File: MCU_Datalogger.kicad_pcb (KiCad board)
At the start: 2 copper layers, 50.2 x 30.2 mm, 30 parts, among them J1 Conn_01x04_Male, J2 Conn_01x04_Male, J3 Conn_01x09_Male, J4 Conn_02x03_Odd_Even, U1 DS1337S+, U2 24LC1025, U3 24LC1025, U4 ATMEGA328P-AU, Y1 32.768 KHz, Y2 16 MHz

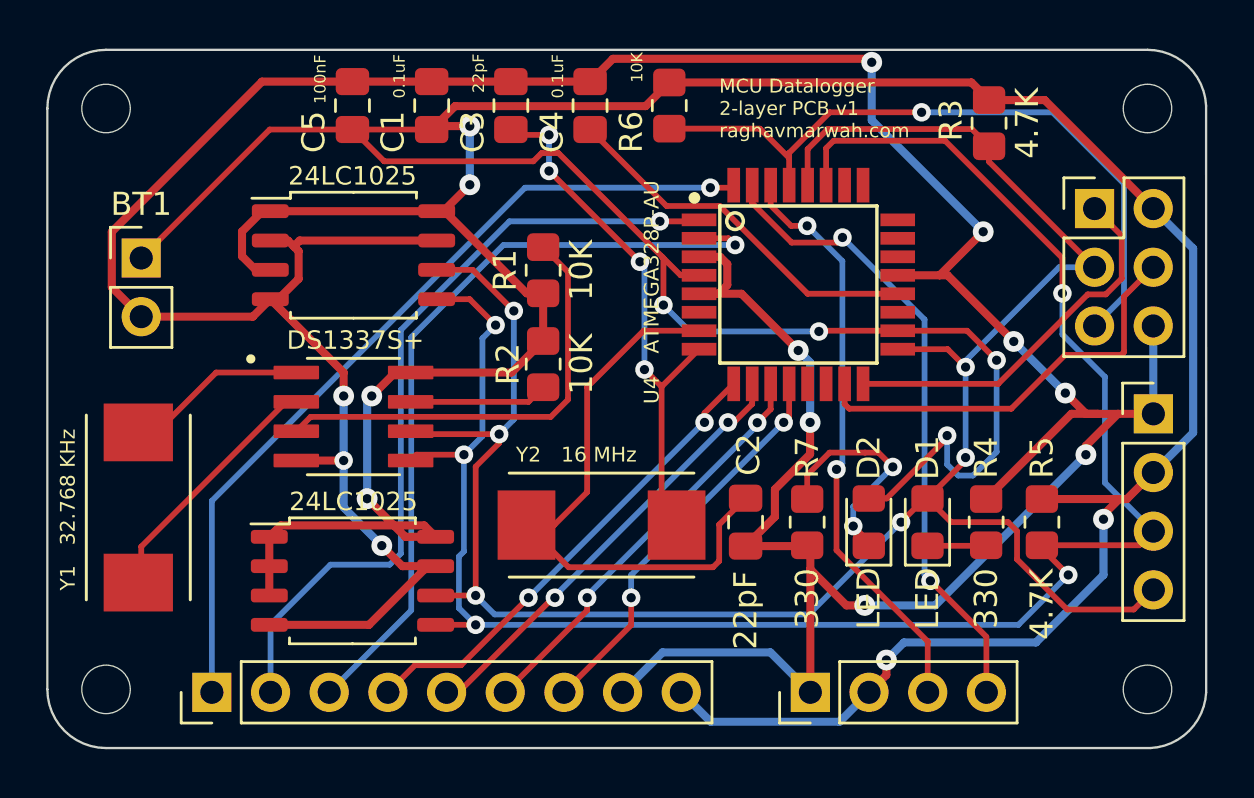
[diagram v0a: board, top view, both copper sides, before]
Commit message: Minor changes to PCB footprints
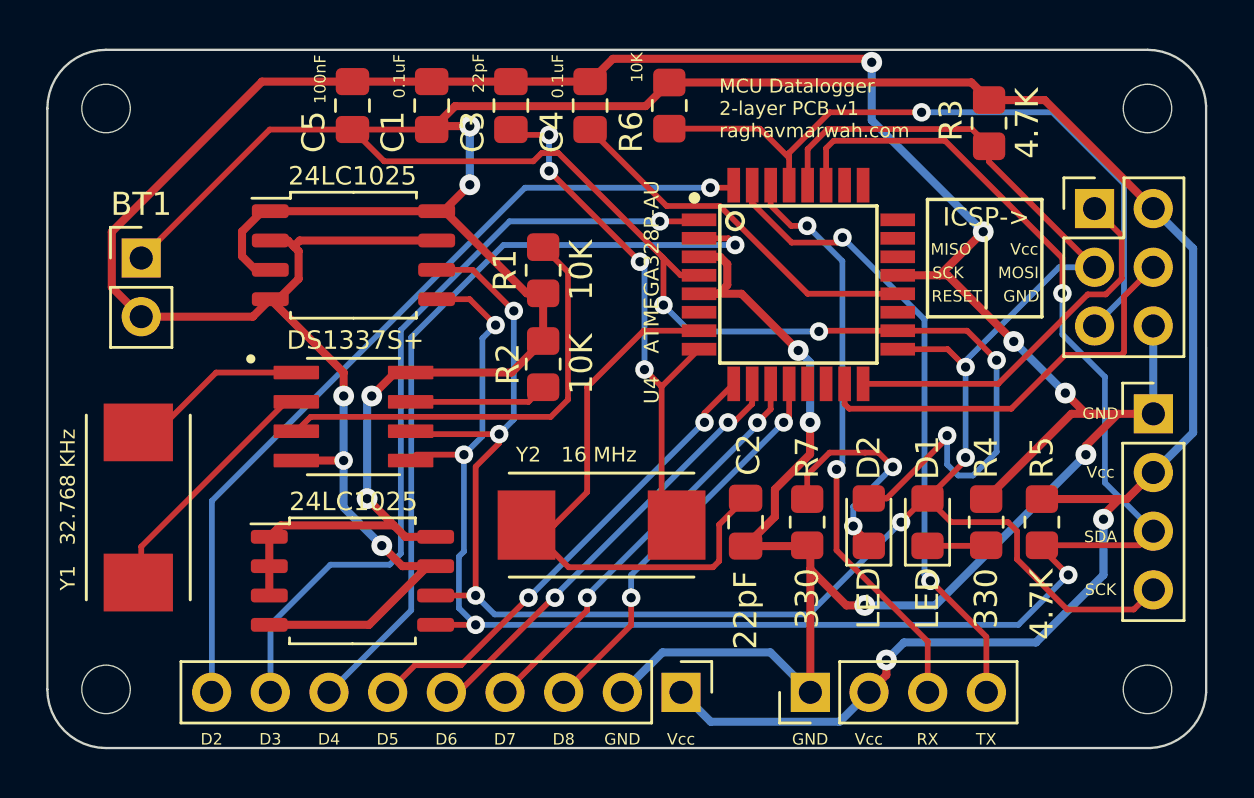
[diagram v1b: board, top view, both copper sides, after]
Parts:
- moved J3 20.3 mm to (153.3, 114.8), turned to -90 degrees
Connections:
- J3 pad 1: /D2 -> /Vcc
- J3 pad 2: /D3 -> GND
- J3 pad 3: /D4 -> /D8
- J3 pad 4: /D5 -> /D7
- J3 pad 6: /D7 -> /D5
- J3 pad 7: /D8 -> /D4
- J3 pad 8: GND -> /D3
- J3 pad 9: /Vcc -> /D2
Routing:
- net /Vcc: track 193.5 -> 191.5 mm
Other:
- board text added: "D2"
- board text added: "D3"
- board text added: "D4"
- board text added: "D5"
- board text added: "D6"
- board text added: "D7"
- board text added: "D8"
- board text added: "GND"
- board text added: "ICSP->"
- board text added: "MISO"
- board text added: "MOSI"
- board text added: "RESET"
- board text added: "RX"
- board text added: "SCK"
- board text added: "SDA"
- board text added: "TX"
- board text added: "Vcc"
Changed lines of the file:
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@@
   )
   (footprint "Connector_PinHeader_2.54mm:PinHeader_1x09_P2.54mm_Vertical" (layer "F.Cu")
-    (at 132.979 114.808 90)
+    (at 153.289 114.808 -90)
     (descr "Through hole straight pin header, 1x09, 2.54mm pitch, single row")
     (tags "Through hole pin header THT 1x09 2.54mm single row")
@@
     (fp_line (start -1.27 -0.635) (end -0.635 -1.27) (layer "F.Fab") (width 0.1))
     (fp_line (start -1.27 21.59) (end -1.27 -0.635) (layer "F.Fab") (width 0.1))
-    (pad "1" thru_hole rect (at 0 0 90) (size 1.7 1.7) (drill 1) (layers *.Cu *.Mask)
-      (net 12 "/D2") (pinfunction "Pin_1") (pintype "passive"))
-    (pad "2" thru_hole oval (at 0 2.54 90) (size 1.7 1.7) (drill 1) (layers *.Cu *.Mask)
-      (net 13 "/D3") (pinfunction "Pin_2") (pintype "passive"))
-    (pad "3" thru_hole oval (at 0 5.08 90) (size 1.7 1.7) (drill 1) (layers *.Cu *.Mask)
-      (net 14 "/D4") (pinfunction "Pin_3") (pintype "passive"))
-    (pad "4" thru_hole oval (at 0 7.62 90) (size 1.7 1.7) (drill 1) (layers *.Cu *.Mask)
-      (net 15 "/D5") (pinfunction "Pin_4") (pintype "passive"))
-    (pad "5" thru_hole oval (at 0 10.16 90) (size 1.7 1.7) (drill 1) (layers *.Cu *.Mask)
+    (pad "1" thru_hole rect (at 0 0 270) (size 1.7 1.7) (drill 1) (layers *.Cu *.Mask)
+      (net 2 "/Vcc") (pinfunction "Pin_1") (pintype "passive"))
+    (pad "2" thru_hole oval (at 0 2.54 270) (size 1.7 1.7) (drill 1) (layers *.Cu *.Mask)
+      (net 1 "GND") (pinfunction "Pin_2") (pintype "passive"))
+    (pad "3" thru_hole oval (at 0 5.08 270) (size 1.7 1.7) (drill 1) (layers *.Cu *.Mask)
+      (net 18 "/D8") (pinfunction "Pin_3") (pintype "passive"))
+    (pad "4" thru_hole oval (at 0 7.62 270) (size 1.7 1.7) (drill 1) (layers *.Cu *.Mask)
+      (net 17 "/D7") (pinfunction "Pin_4") (pintype "passive"))
+    (pad "5" thru_hole oval (at 0 10.16 270) (size 1.7 1.7) (drill 1) (layers *.Cu *.Mask)
       (net 16 "/D6") (pinfunction "Pin_5") (pintype "passive"))
-    (pad "6" thru_hole oval (at 0 12.7 90) (size 1.7 1.7) (drill 1) (layers *.Cu *.Mask)
-      (net 17 "/D7") (pinfunction "Pin_6") (pintype "passive"))
-    (pad "7" thru_hole oval (at 0 15.24 90) (size 1.7 1.7) (drill 1) (layers *.Cu *.Mask)
-      (net 18 "/D8") (pinfunction "Pin_7") (pintype "passive"))
-    (pad "8" thru_hole oval (at 0 17.78 90) (size 1.7 1.7) (drill 1) (layers *.Cu *.Mask)
-      (net 1 "GND") (pinfunction "Pin_8") (pintype "passive"))
-    (pad "9" thru_hole oval (at 0 20.32 90) (size 1.7 1.7) (drill 1) (layers *.Cu *.Mask)
-      (net 2 "/Vcc") (pinfunction "Pin_9") (pintype "passive"))
+    (pad "6" thru_hole oval (at 0 12.7 270) (size 1.7 1.7) (drill 1) (layers *.Cu *.Mask)
+      (net 15 "/D5") (pinfunction "Pin_6") (pintype "passive"))
+    (pad "7" thru_hole oval (at 0 15.24 270) (size 1.7 1.7) (drill 1) (layers *.Cu *.Mask)
+      (net 14 "/D4") (pinfunction "Pin_7") (pintype "passive"))
+    (pad "8" thru_hole oval (at 0 17.78 270) (size 1.7 1.7) (drill 1) (layers *.Cu *.Mask)
+      (net 13 "/D3") (pinfunction "Pin_8") (pintype "passive"))
+    (pad "9" thru_hole oval (at 0 20.32 270) (size 1.7 1.7) (drill 1) (layers *.Cu *.Mask)
+      (net 12 "/D2") (pinfunction "Pin_9") (pintype "passive"))
     (model "${KICAD6_3DMODEL_DIR}/Connector_PinHeader_2.54mm.3dshapes/PinHeader_1x09_P2.54mm_Vertical.wrl"
       (offset (xyz 0 0 0))
@@
       ) (layer "B.SilkS") (width 0.01) (fill solid))
   )
+  (gr_line (start 166.497 95.123) (end 166.497 98.171) (layer "F.SilkS") (width 0.15))
+  (gr_rect (start 163.957 93.472) (end 168.91 98.552) (layer "F.SilkS") (width 0.15) (fill none))
   (gr_arc (start 125.857 89.535) (mid 126.600949 87.738949) (end 128.397 86.995) (layer "Edge.Cuts") (width 0.1))
   (gr_line (start 125.857 89.535) (end 125.857 114.681) (layer "Edge.Cuts") (width 0.1))
@@
   (gr_line (start 128.397 117.221) (end 173.609 117.221) (layer "Edge.Cuts") (width 0.1))
   (gr_rect (start 125.857 86.995) (end 175.9966 117.1956) (layer "User.2") (width 0.1) (fill none))
+  (gr_text "MOSI" (at 167.894 96.647) (layer "F.SilkS")
+    (effects (font (size 0.5 0.5) (thickness 0.08)))
+  )
+  (gr_text "GND" (at 168.021 97.663) (layer "F.SilkS")
+    (effects (font (size 0.5 0.5) (thickness 0.08)))
+  )
+  (gr_text "TX" (at 166.497 116.84) (layer "F.SilkS")
+    (effects (font (size 0.5 0.5) (thickness 0.1)))
+  )
+  (gr_text "GND\n" (at 158.877 116.84) (layer "F.SilkS")
+    (effects (font (size 0.5 0.5) (thickness 0.1)))
+  )
+  (gr_text "Vcc" (at 168.148 95.631) (layer "F.SilkS")
+    (effects (font (size 0.5 0.5) (thickness 0.08)))
+  )
+  (gr_text "Vcc" (at 153.289 116.84) (layer "F.SilkS")
+    (effects (font (size 0.5 0.5) (thickness 0.1)))
+  )
+  (gr_text "MISO" (at 164.973 95.631) (layer "F.SilkS")
+    (effects (font (size 0.5 0.5) (thickness 0.08)))
+  )
+  (gr_text "SDA" (at 171.45 108.077) (layer "F.SilkS")
+    (effects (font (size 0.5 0.5) (thickness 0.1)))
+  )
+  (gr_text "SCK" (at 171.45 110.363) (layer "F.SilkS")
+    (effects (font (size 0.5 0.5) (thickness 0.1)))
+  )
+  (gr_text "D2" (at 132.969 116.84) (layer "F.SilkS")
+    (effects (font (size 0.5 0.5) (thickness 0.1)))
+  )
+  (gr_text "GND\n" (at 171.45 102.743) (layer "F.SilkS")
+    (effects (font (size 0.5 0.5) (thickness 0.1)))
+  )
   (gr_text "MCU Datalogger\n2-layer PCB v1\nraghavmarwah.com" (at 154.94 89.535) (layer "F.SilkS")
     (effects (font (size 0.6 0.6) (thickness 0.12)) (justify left))
   )
+  (gr_text "GND\n" (at 150.749 116.84) (layer "F.SilkS")
+    (effects (font (size 0.5 0.5) (thickness 0.1)))
+  )
+  (gr_text "D8" (at 148.209 116.84) (layer "F.SilkS")
+    (effects (font (size 0.5 0.5) (thickness 0.1)))
+  )
+  (gr_text "RX" (at 163.957 116.84) (layer "F.SilkS")
+    (effects (font (size 0.5 0.5) (thickness 0.1)))
+  )
+  (gr_text "Vcc" (at 161.417 116.84) (layer "F.SilkS")
+    (effects (font (size 0.5 0.5) (thickness 0.1)))
+  )
+  (gr_text "D3" (at 135.509 116.84) (layer "F.SilkS")
+    (effects (font (size 0.5 0.5) (thickness 0.1)))
+  )
+  (gr_text "Vcc" (at 171.45 105.283) (layer "F.SilkS")
+    (effects (font (size 0.5 0.5) (thickness 0.1)))
+  )
+  (gr_text "ICSP->" (at 166.497 94.234) (layer "F.SilkS")
+    (effects (font (size 0.8 0.8) (thickness 0.1)))
+  )
+  (gr_text "D5" (at 140.589 116.84) (layer "F.SilkS")
+    (effects (font (size 0.5 0.5) (thickness 0.1)))
+  )
+  (gr_text "SCK" (at 164.846 96.647) (layer "F.SilkS")
+    (effects (font (size 0.5 0.5) (thickness 0.08)))
+  )
+  (gr_text "D7" (at 145.669 116.84) (layer "F.SilkS")
+    (effects (font (size 0.5 0.5) (thickness 0.1)))
+  )
+  (gr_text "RESET" (at 165.227 97.663) (layer "F.SilkS")
+    (effects (font (size 0.5 0.5) (thickness 0.08)))
+  )
+  (gr_text "D4" (at 138.049 116.84) (layer "F.SilkS")
+    (effects (font (size 0.5 0.5) (thickness 0.1)))
+  )
+  (gr_text "D6" (at 143.129 116.84) (layer "F.SilkS")
+    (effects (font (size 0.5 0.5) (thickness 0.1)))
+  )
   (segment (start 138.684 100.965) (end 138.684 101.981) (width 0.35) (layer "F.Cu") (net 1))
   (segment (start 164.827 96.755) (end 167.69199 99.61999) (width 0.35) (layer "F.Cu") (net 1))
@@
   (segment (start 164.8085 103.7965) (end 162.188 106.417) (width 0.25) (layer "F.Cu") (net 2))
   (segment (start 152.4635 95.9485) (end 153.27 96.755) (width 0.25) (layer "F.Cu") (net 2))
+  (segment (start 135.959 107.583) (end 135.465 108.077) (width 0.35) (layer "F.Cu") (net 2))
   (segment (start 151.756 89.433) (end 152.781 88.408) (width 0.35) (layer "F.Cu") (net 2))
   (segment (start 144.145 90.297) (end 142.6425 90.297) (width 0.35) (layer "F.Cu") (net 2))
@@
   (segment (start 143.052173 93.98) (end 146.608173 97.536) (width 0.35) (layer "F.Cu") (net 2))
   (segment (start 135.465 108.077) (end 135.465 110.617) (width 0.35) (layer "F.Cu") (net 2))
-  (segment (start 135.959 107.583) (end 135.465 108.077) (width 0.35) (layer "F.Cu") (net 2))
   (segment (start 159.29 99.155) (end 162.669 99.155) (width 0.25) (layer "F.Cu") (net 2))
   (segment (start 171.577 107.1245) (end 171.577 107.315) (width 0.35) (layer "F.Cu") (net 2))
@@
   (segment (start 147.252984 91.4645) (end 147.9795 91.4645) (width 0.25) (layer "F.Cu") (net 2))
   (segment (start 134.284 94.861827) (end 134.284 95.93) (width 0.35) (layer "F.Cu") (net 2))
-  (segment (start 142.665 108.077) (end 142.171 107.583) (width 0.35) (layer "F.Cu") (net 2))
   (segment (start 152.781 88.408) (end 165.862 88.408) (width 0.35) (layer "F.Cu") (net 2))
-  (segment (start 142.171 107.583) (end 135.959 107.583) (width 0.35) (layer "F.Cu") (net 2))
   (segment (start 142.709 93.98) (end 143.052173 93.98) (width 0.35) (layer "F.Cu") (net 2))
   (segment (start 135.509 93.98) (end 135.165827 93.98) (width 0.35) (layer "F.Cu") (net 2))
+  (segment (start 140.843 107.583) (end 135.959 107.583) (width 0.35) (layer "F.Cu") (net 2))
   (segment (start 139.7 106.426) (end 141.351 108.077) (width 0.35) (layer "F.Cu") (net 2))
   (segment (start 141.351 108.077) (end 142.665 108.077) (width 0.35) (layer "F.Cu") (net 2))

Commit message: Added SCL net to schematic and fixed errors
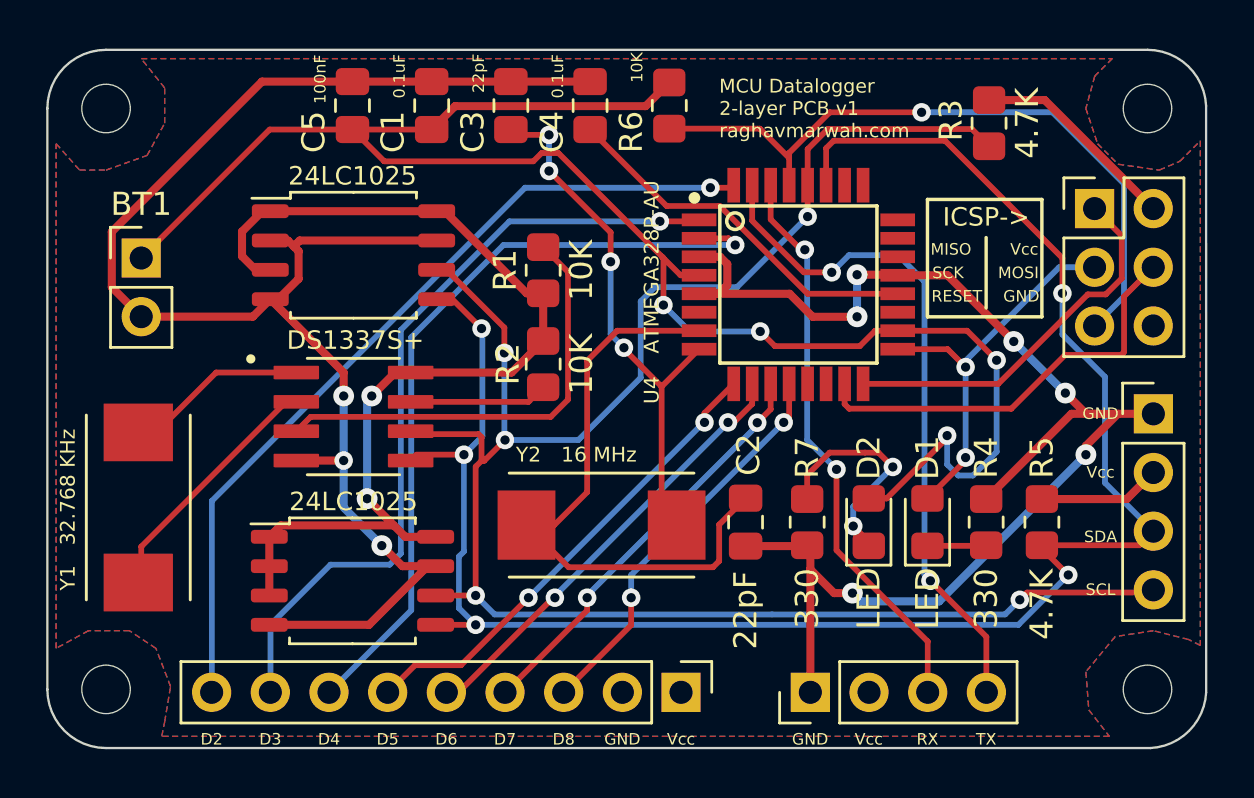
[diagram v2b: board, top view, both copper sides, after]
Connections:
- J1 pad 4: /SCK -> /SCL
- R3 pad 2: /SCK -> /SCL
- U1 pad 6: /SCK -> /SCL
- U2 pad 6: /SCK -> /SCL
- U3 pad 6: /SCK -> /SCL
- U4 pad 28: /SCK -> /SCL
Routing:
- net /SCL: track 0.00 -> 81.8 mm, vias 0 -> 5
- net /SCK: track 91.6 -> 16.9 mm, vias 6 -> 2
- net /Vcc: track 191.5 -> 133.6 mm, vias 10 -> 6
- net GND: track 173.1 -> 130.6 mm, vias 11 -> 9
- net /TX: track 27.8 -> 29.6 mm
- net /SDA: track 82.0 -> 81.1 mm
- net Net-(C2-Pad2): track 25.4 -> 26.0 mm
- net /RX: track 25.4 -> 24.9 mm
- added copper zone on F.Cu, net /Vcc
- added copper zone on B.Cu, net GND
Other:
- board text added: "SCL"

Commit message: Test commit, deleted tracks and vias
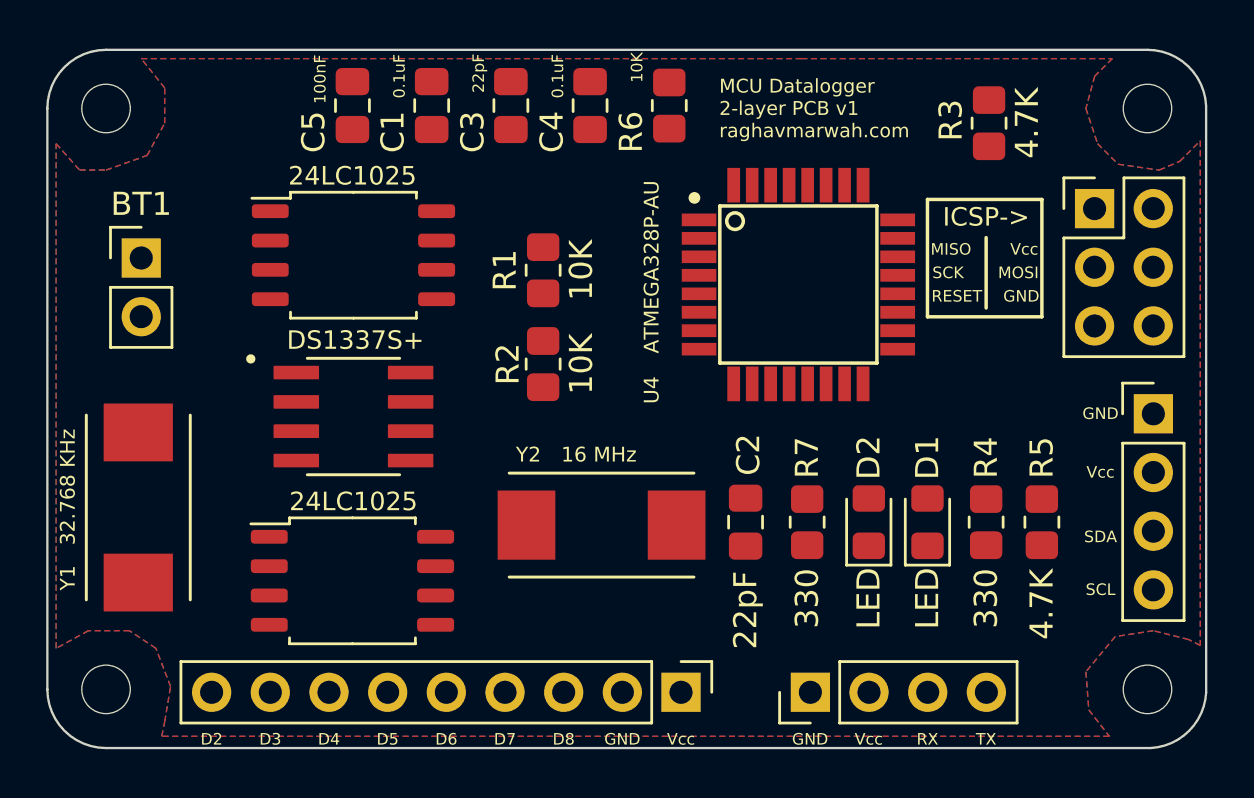
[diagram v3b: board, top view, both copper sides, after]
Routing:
- net /Vcc: track 133.6 -> 0.00 mm, vias 6 -> 0
- net GND: track 130.6 -> 0.00 mm, vias 9 -> 0
- net /SCL: track 81.8 -> 0.00 mm, vias 5 -> 0
- net /SDA: track 81.1 -> 0.00 mm, vias 5 -> 0
- net /D2: track 36.5 -> 0.00 mm, vias 1 -> 0
- net /D3: track 34.4 -> 0.00 mm, vias 1 -> 0
- net /D4: track 34.2 -> 0.00 mm, vias 1 -> 0
- net /RESET: track 30.3 -> 0.00 mm, vias 1 -> 0
- net /TX: track 29.6 -> 0.00 mm, vias 2 -> 0
- net Net-(C2-Pad2): track 26.0 -> 0.00 mm
- net /RX: track 24.9 -> 0.00 mm, vias 2 -> 0
- net Net-(C3-Pad2): track 23.0 -> 0.00 mm, vias 4 -> 0
- net /D5: track 20.7 -> 0.00 mm, vias 2 -> 0
- net Net-(R1-Pad2): track 19.4 -> 0.00 mm
- net /D6: track 19.3 -> 0.00 mm, vias 2 -> 0
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
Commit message: 4 layer PCB design complete
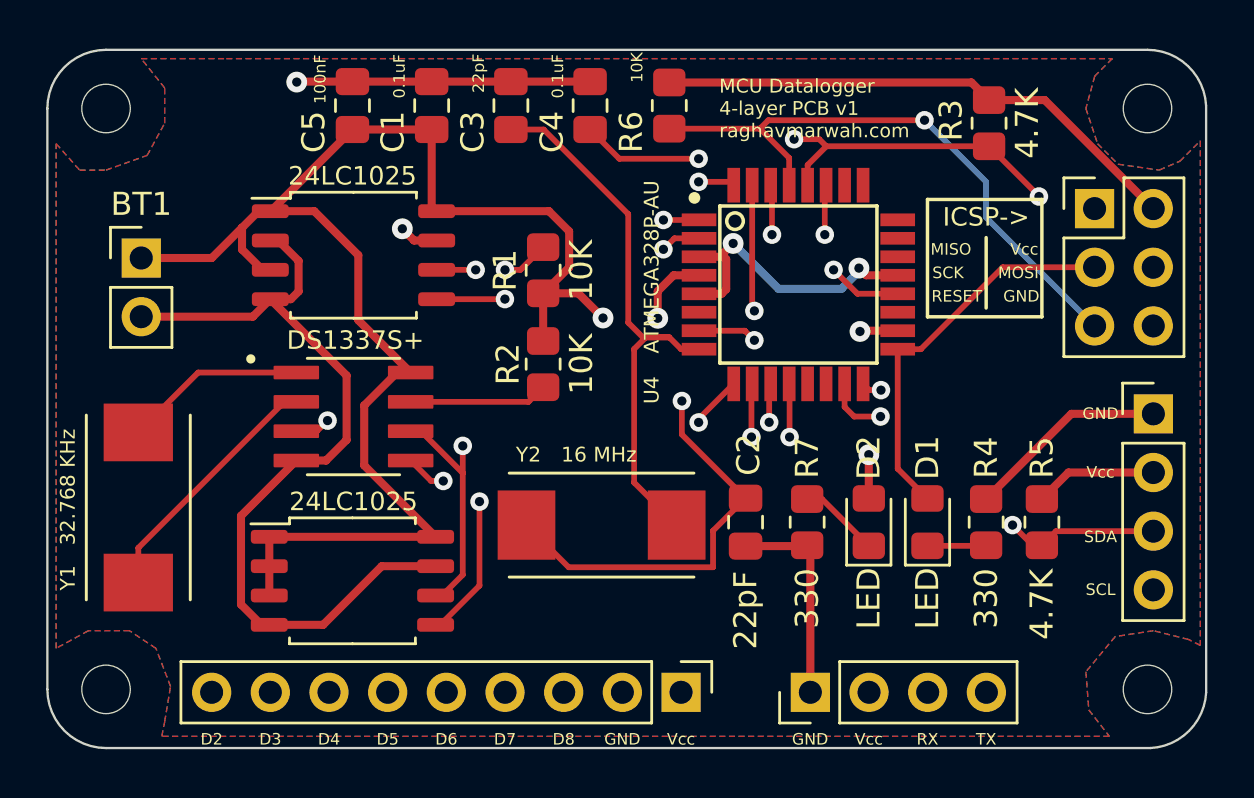
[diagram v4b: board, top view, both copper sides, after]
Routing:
- net /Vcc: track 0.00 -> 118.4 mm, vias 0 -> 4
- net GND: track 0.00 -> 82.6 mm, vias 0 -> 4
- net /SCL: track 0.00 -> 71.0 mm, vias 0 -> 4
- net /SDA: track 0.00 -> 69.0 mm, vias 0 -> 5
- net /D2: track 0.00 -> 33.7 mm, vias 0 -> 1
- net /D3: track 0.00 -> 29.0 mm, vias 0 -> 1
- net /D4: track 0.00 -> 26.9 mm, vias 0 -> 1
- net /TX: track 0.00 -> 26.2 mm, vias 0 -> 1
- net /RESET: track 0.00 -> 26.1 mm, vias 0 -> 1
- net /RX: track 0.00 -> 26.0 mm, vias 0 -> 1
- net Net-(C3-Pad2): track 0.00 -> 25.0 mm
- net Net-(C2-Pad2): track 0.00 -> 24.5 mm, vias 0 -> 2
- net /D5: track 0.00 -> 22.4 mm, vias 0 -> 1
- net /D6: track 0.00 -> 21.9 mm, vias 0 -> 1
- net /D7: track 0.00 -> 20.3 mm, vias 0 -> 1
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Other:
- copper layers 2 -> 4
- board text added: "MCU Datalogger 4-layer PCB v1 raghavmarwah.com"
- board text removed: "MCU Datalogger 2-layer PCB v1 raghavmarwah.com"
